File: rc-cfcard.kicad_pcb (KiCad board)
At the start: 2 copper layers, 99.1 x 49.9 mm, 14 parts, among them J1 RC2014, J2 RC2014_Enh, J3 CF Socket, U1 74AHCT138, U2 74HCT32, U3 74HC245

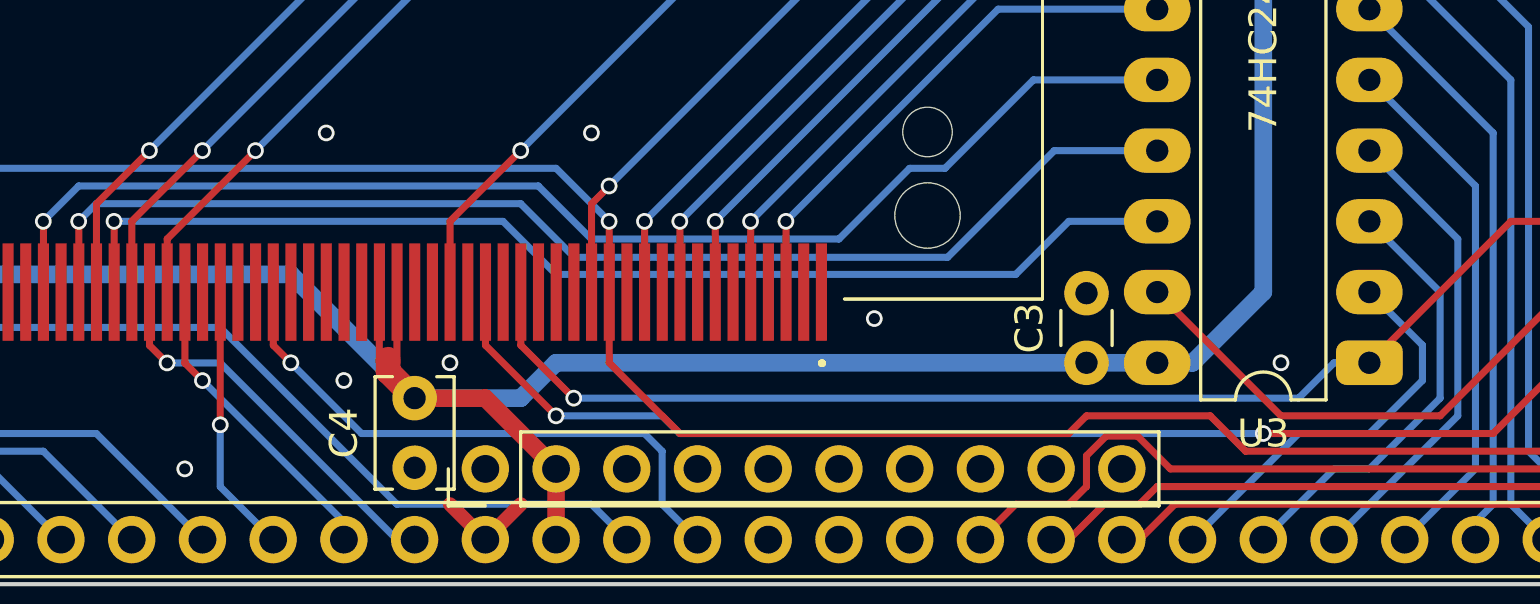
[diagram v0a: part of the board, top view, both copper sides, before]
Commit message: Fix footprint reference
Fix footprint reference, clean up groundplane routing a little
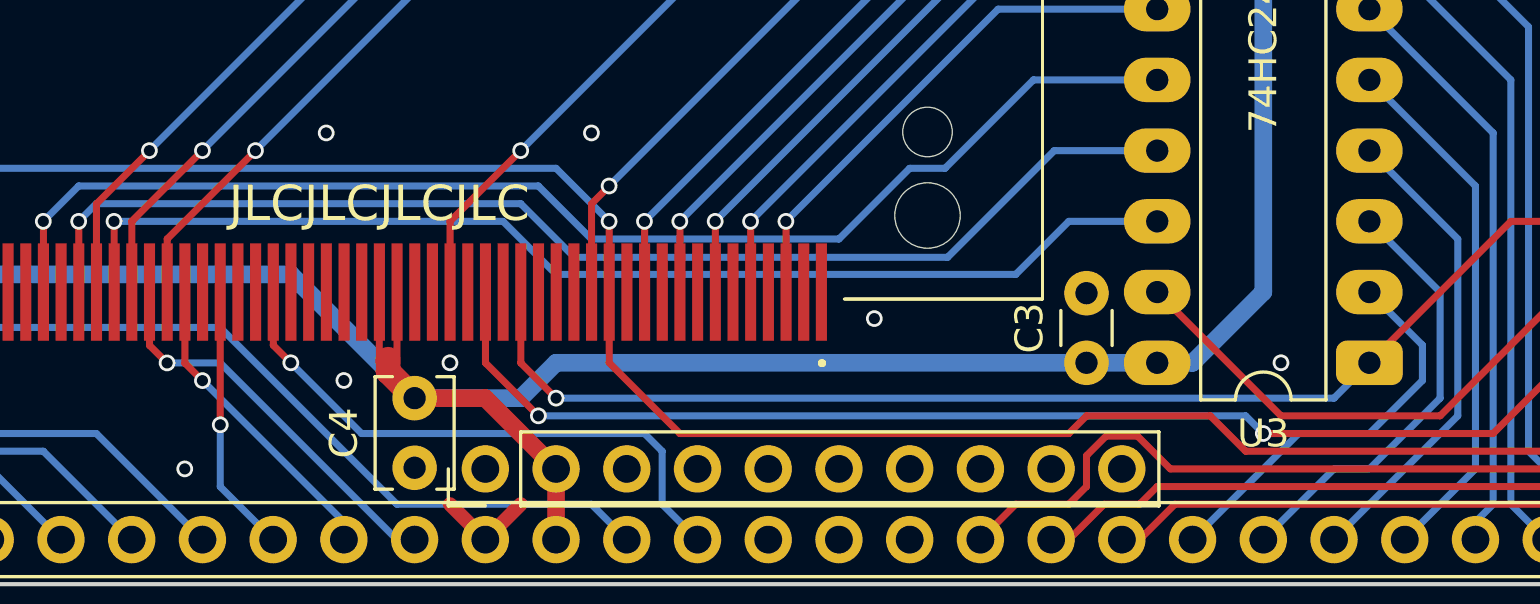
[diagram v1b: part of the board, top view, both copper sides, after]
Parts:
- J3: footprint PD_Parts:CF_Card_Socket -> rc-cfcard:CF_Card_Socket
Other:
- board text added: "JLCJLCJLCJLC"

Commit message: Replace resistor network with SMT parts
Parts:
- removed RN1: 1k, Resistor_THT:R_Array_SIP5
- added R2: 1k, Resistor_SMD:R_0805_2012Metric, F.Cu at (199.1, 144.8)
- added R3: 1k, Resistor_SMD:R_0805_2012Metric, F.Cu at (193.0, 144.8)
- added R4: 1k, Resistor_SMD:R_0805_2012Metric, F.Cu at (182.9, 145.7)
- added R5: 1k, Resistor_SMD:R_0805_2012Metric, F.Cu at (180.3, 145.7)
- C4: footprint Capacitor_THT:C_Disc_D3.8mm_W2.6mm_P2.50mm -> Capacitor_SMD:C_0805_2012Metric
- moved C4 1.92 mm to (189.9, 144.5), turned to 180 degrees
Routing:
- net /~PDIAG: track 52.1 -> 3.83 mm, vias 1 -> 0
- net /~DMACK: track 50.3 -> 3.81 mm, vias 1 -> 0
- net /~WE: track 43.0 -> 2.87 mm, vias 1 -> 0
- net /~CS1: track 40.8 -> 3.81 mm, vias 1 -> 0
- net +5V: track 157.7 -> 180.2 mm, vias 1 -> 4
- net /~ACT: track 75.7 -> 72.5 mm
- net A3: track 40.9 -> 43.7 mm
- net A4: track 37.3 -> 39.2 mm
- net ~CFCS: track 89.9 -> 90.9 mm
- net A5: track 33.7 -> 34.7 mm
- net ~RESET: track 21.2 -> 21.7 mm
- net GND: vias 20 -> 19
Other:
- board text added: "CompactFlash Adapter Card PD105S v1.0"
- board text removed: "CompactFlash Adapter Card PD105 v0.9"

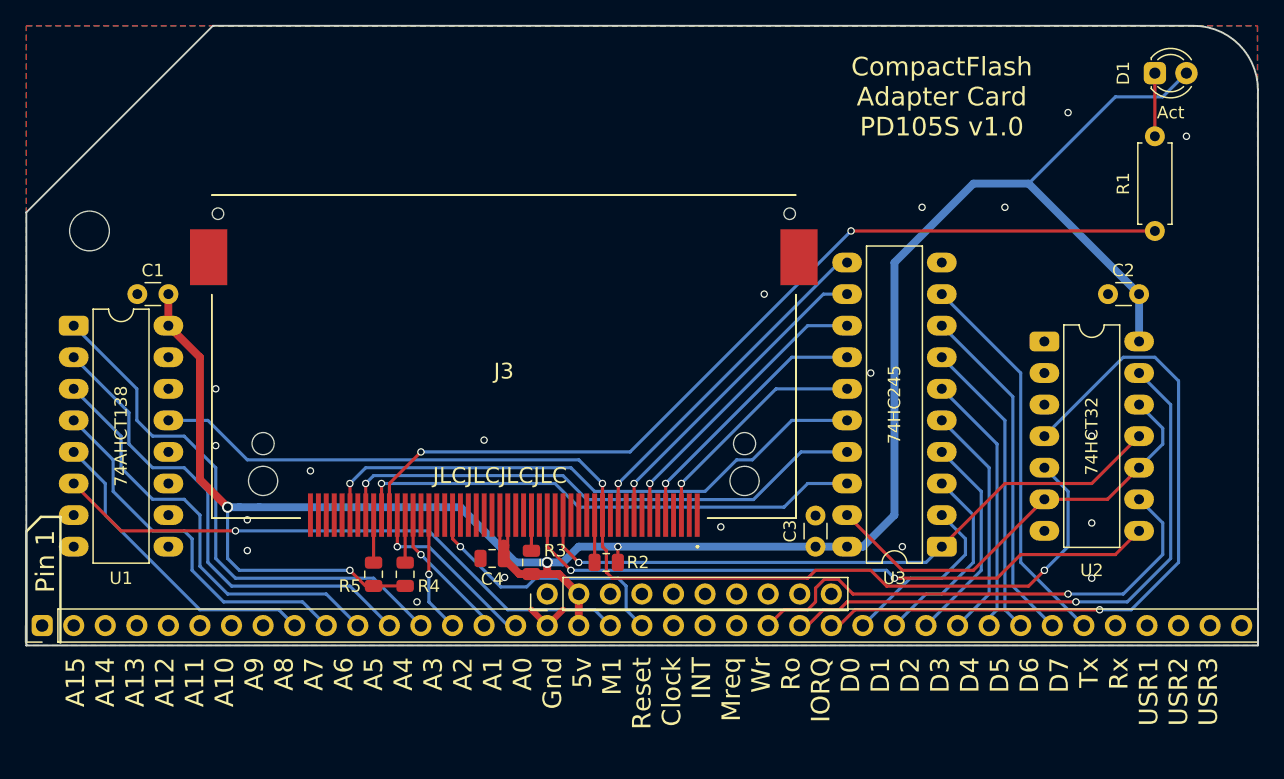
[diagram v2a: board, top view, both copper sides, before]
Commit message: Change to through-hole CF socket
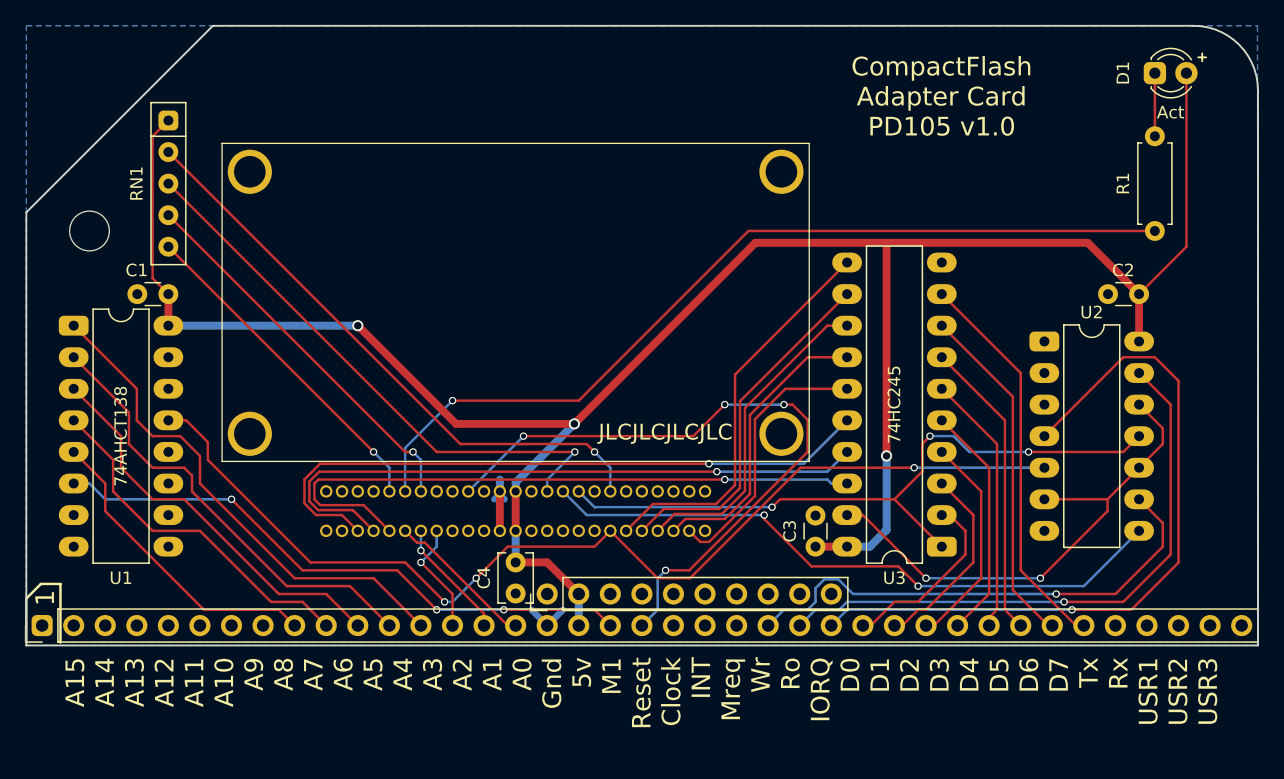
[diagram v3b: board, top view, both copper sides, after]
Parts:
- removed R2, R3, R4, R5: 1k, Resistor_SMD:R_0805_2012Metric
- added RN1: 1k, Resistor_THT:R_Array_SIP5, F.Cu at (163.8, 109.2)
- C4: footprint Capacitor_SMD:C_0805_2012Metric -> Capacitor_THT:C_Disc_D3.8mm_W2.6mm_P2.50mm
- J3: footprint rc-cfcard:CF_Card_Socket -> rc-cfcard:CF_Card_Socket_PTH
- R1: value 470R -> 330R
- moved J3 3.91 mm to (191.8, 134.4)
- moved C4 1.92 mm to (191.8, 144.8), turned to 270 degrees
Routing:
- net /~CS1: track 3.81 -> 48.0 mm, vias 0 -> 1
- net /~WE: track 2.87 -> 45.7 mm, vias 0 -> 1
- net ~RESET: track 21.7 -> 53.9 mm, vias 1 -> 4
- net /~DMACK: track 3.81 -> 31.0 mm, vias 0 -> 1
- net /~PDIAG: track 3.83 -> 27.0 mm, vias 0 -> 1
- net D0': track 41.6 -> 51.5 mm
- net D1': track 43.9 -> 52.0 mm
- net D2': track 46.2 -> 52.8 mm
- net ~IOCS: track 35.4 -> 41.6 mm, vias 0 -> 2
- net ~CFCS: track 90.9 -> 85.0 mm, vias 2 -> 3
- net GND: track 3.59 -> 8.62 mm, vias 19 -> 0
- net D7': track 28.3 -> 31.9 mm, vias 1 -> 0
- net A3: track 43.7 -> 40.7 mm
- net D3': track 19.0 -> 21.8 mm, vias 1 -> 0
- net A0: track 14.7 -> 12.0 mm, vias 1 -> 0
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- removed copper zone on F.Cu, net GND
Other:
- board text added: "1"
- board text added: "CompactFlash Adapter Card PD105 v1.0"
- board text removed: "CompactFlash Adapter Card PD105S v1.0"
- board text removed: "Pin 1"

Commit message: Re-arranged support chips
Moved buffer and OR gate so that data traces can be more uniform in length
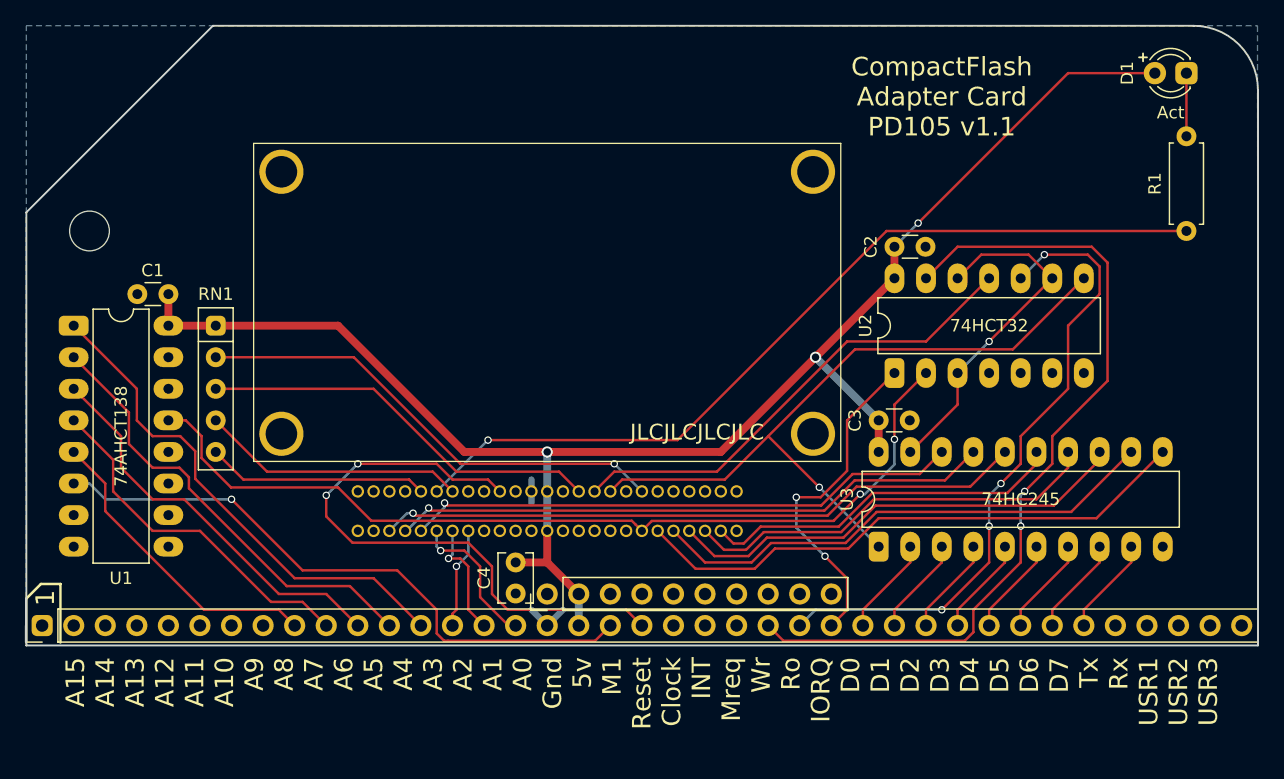
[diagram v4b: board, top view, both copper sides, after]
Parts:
- moved C2 20.1 mm to (222.2, 119.4), turned to 0 degrees
- moved RN1 16.9 mm to (167.6, 125.7)
- moved U2 12.3 mm to (222.2, 129.5), turned to 90 degrees
- moved C3 11.4 mm to (221.0, 133.3), turned to 0 degrees
- moved U3 5.08 mm to (221.0, 143.5), turned to 90 degrees
- moved D1 2.54 mm to (245.7, 105.4), turned to 180 degrees
- moved J3 2.54 mm to (194.3, 134.4)
- moved R1 2.54 mm to (245.7, 110.5)
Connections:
- U2 pad 1: GND -> ~IOREQ
- U2 pad 10: ~IOCS -> ~RD
- U2 pad 11: ~IORD -> ~IOWR
- U2 pad 13: ~RD -> ~WR
- U2 pad 2: GND -> ~CFCS
- U2 pad 3: Net-(U2-Pad3) -> ~IOCS
- U2 pad 4: ~IOREQ -> GND
- U2 pad 5: ~CFCS -> GND
- U2 pad 6: ~IOCS -> Net-(U2-Pad6)
- U2 pad 8: ~IOWR -> ~IORD
- U2 pad 9: ~WR -> ~IOCS
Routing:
- net +5V: track 181.0 -> 127.5 mm
- net ~IOREQ: track 58.9 -> 27.0 mm, vias 1 -> 2
- net ~WR: track 40.6 -> 67.7 mm, vias 1 -> 2
- net D7: track 32.5 -> 8.61 mm
- net D6: track 28.0 -> 7.93 mm
- net D5: track 24.2 -> 7.93 mm
- net D7': track 31.9 -> 45.8 mm
- net ~IOCS: track 41.6 -> 27.9 mm, vias 2 -> 1
- net D4: track 21.2 -> 7.93 mm
- net /~WE: track 45.7 -> 32.6 mm, vias 1 -> 0
- net D6': track 28.5 -> 41.6 mm
- net ~IOWR: track 51.5 -> 38.9 mm, vias 2 -> 0
- net D5': track 26.0 -> 37.7 mm
- net ~CFCS: track 85.0 -> 73.8 mm, vias 3 -> 2
- net D3: track 19.1 -> 7.93 mm
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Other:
- rule pad_to_mask_clearance: 0.127 -> 0
- board text added: "CompactFlash Adapter Card PD105 v1.1"
- board text removed: "CompactFlash Adapter Card PD105 v1.0"
